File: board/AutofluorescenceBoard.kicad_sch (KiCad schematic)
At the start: 38 parts, among them U1 PAM2863ECR, U2 PAM2863ECR, U3 PAM2863ECR

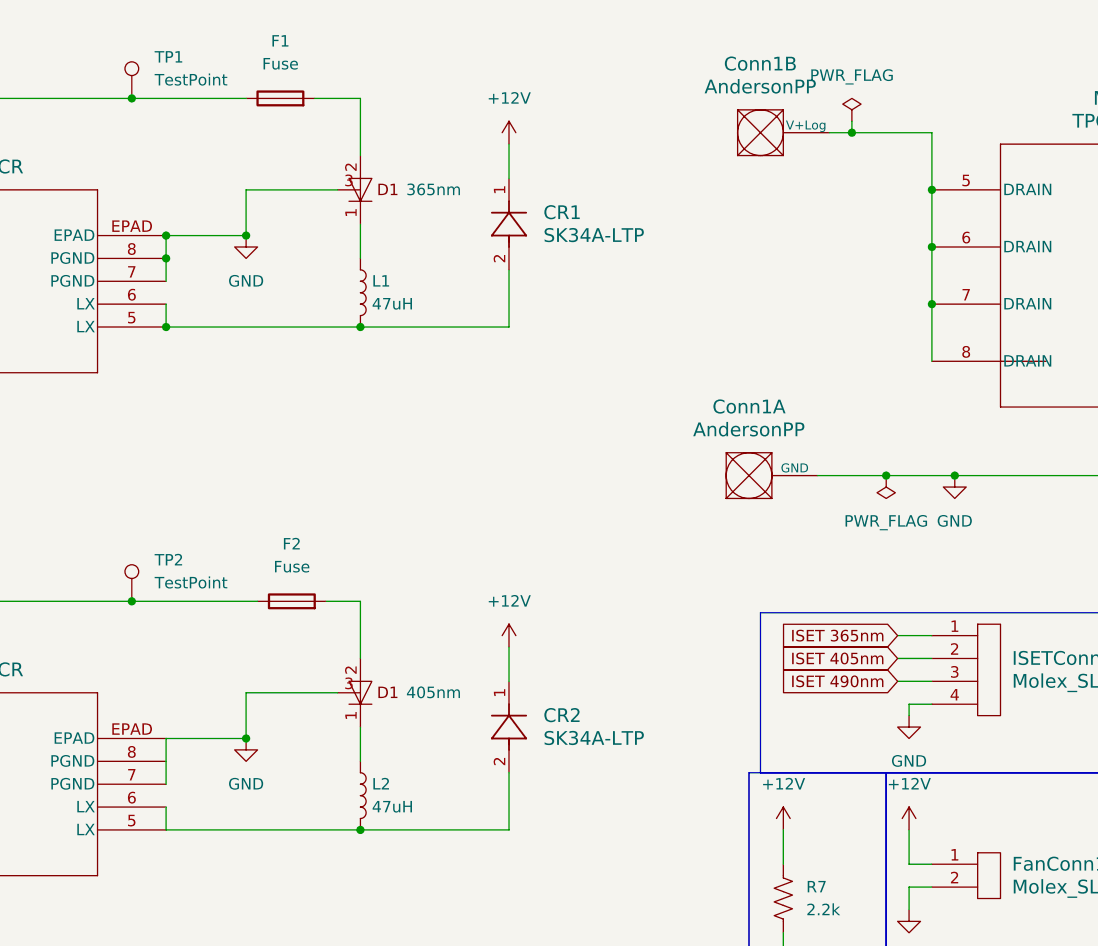
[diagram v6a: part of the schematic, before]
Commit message: Layout Ground Fixes
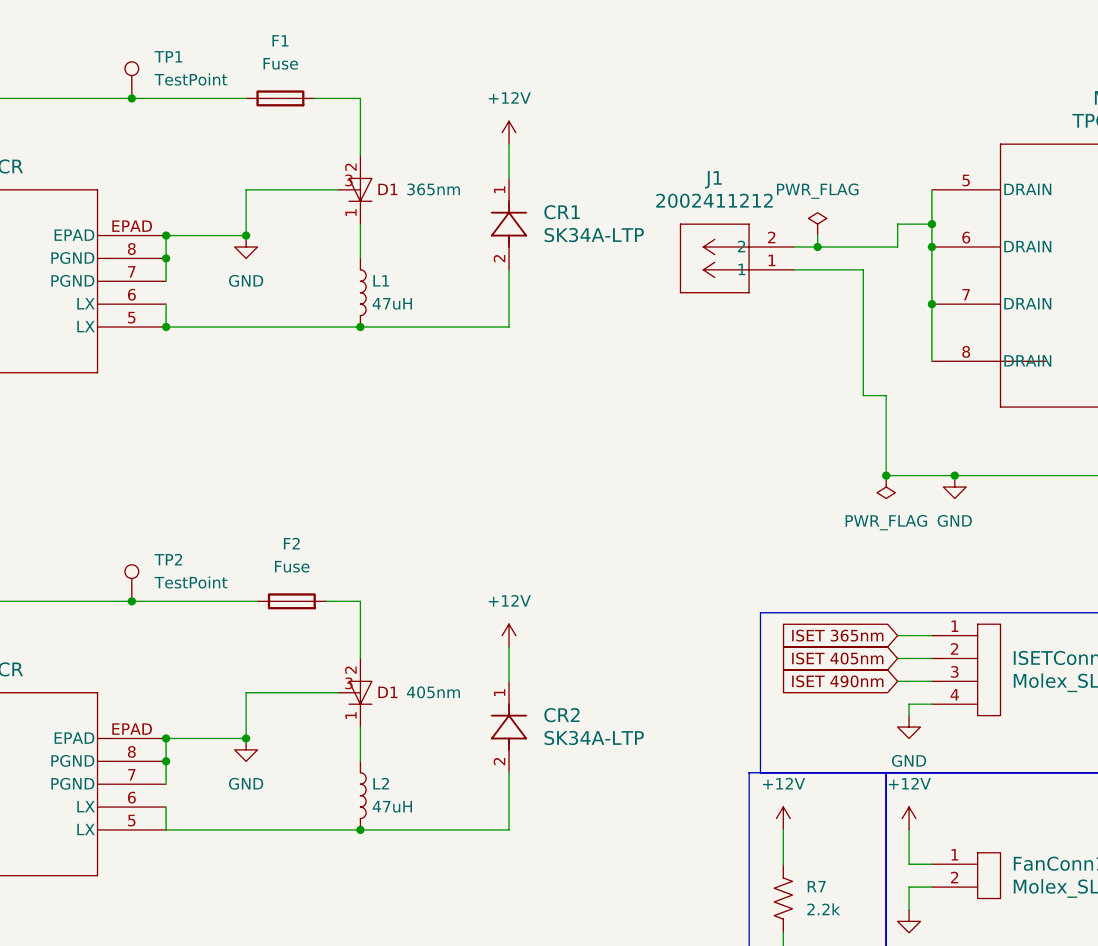
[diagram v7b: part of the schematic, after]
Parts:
- removed Conn1: AndersonPP, MRDT_Connectors:Square_Anderson_2_H_Side_By_Side, symbol MRDT_Connectors:AndersonPP
- added J1: 2002411212, CONN_2002412000_02_MOL, symbol AutofluorescenceBoard:2002411212
- FanConn1: footprint MRDT_Connectors:MOLEX_SL_02_Horizontal -> MRDT_Connectors:MOLEX_SL_02_Vertical
- ISETConn1: footprint MRDT_Connectors:MOLEX_SL_04_Horizontal -> MRDT_Connectors:MOLEX_SL_04_Vertical
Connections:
- net GND: now also U2.8 (PGND), J1.1
- net at MOSFET1.5 (DRAIN), MOSFET1.6 (DRAIN), MOSFET1.7 (DRAIN)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: now also J1.2

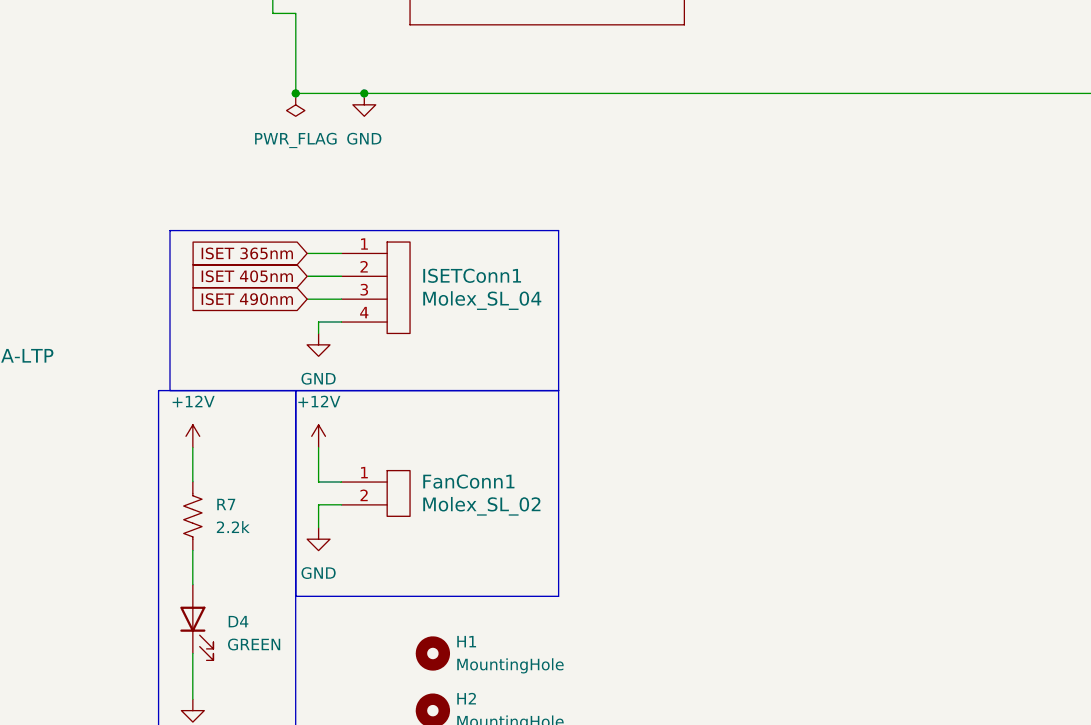
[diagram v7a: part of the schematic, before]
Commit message: Added White LED
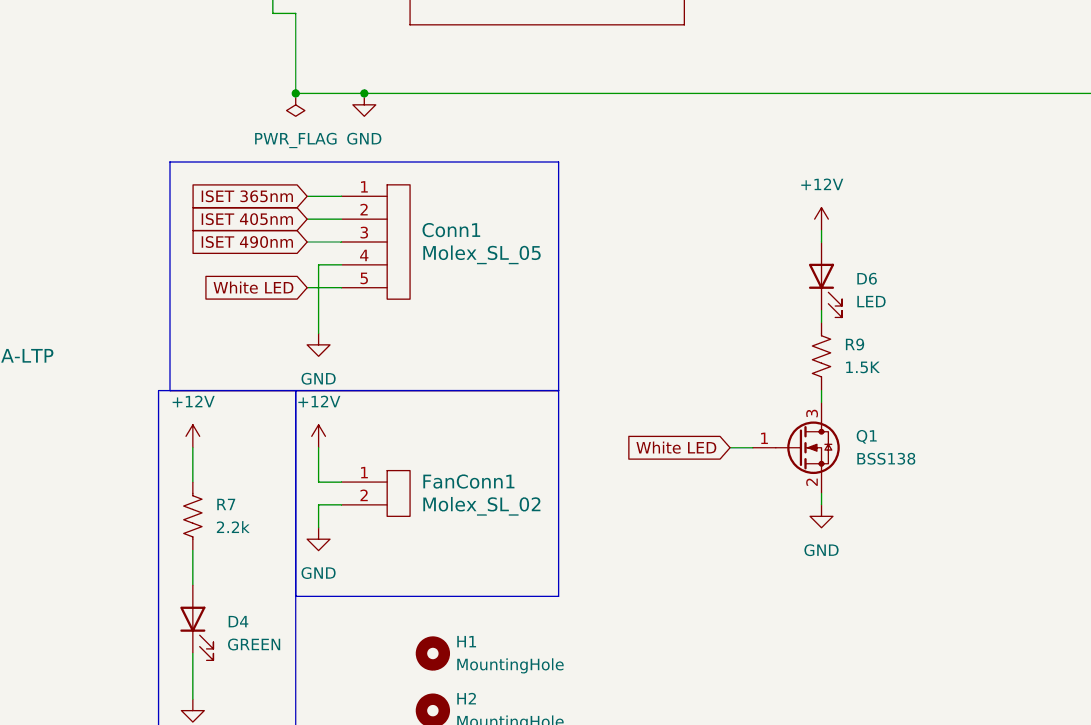
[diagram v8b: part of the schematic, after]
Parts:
- removed ISETConn1: Molex_SL_04, MRDT_Connectors:MOLEX_SL_04_Vertical, symbol MRDT_Connectors:Molex_SL_04
- added Conn1: Molex_SL_05, AutofluorescenceBoard:MOLEX_SL_05_Vertical_AF, symbol MRDT_Connectors:Molex_SL_05
- added D6: LED, AutofluorescenceBoard:INS63AT5UW, symbol Device:LED
- added Q1: BSS138, Package_TO_SOT_SMD:SOT-23, symbol Transistor_FET:BSS138
- added R9: 1.5K, AutofluorescenceBoard:RES_R0603_ROM-M, symbol Device:R_US
- FanConn1: footprint MRDT_Connectors:MOLEX_SL_02_Vertical -> AutofluorescenceBoard:MOLEX_SL_02_Horizontal
- J1: footprint CONN_2002412000_02_MOL -> AutofluorescenceBoard:CONN_SD-172286-1000_02_MOL
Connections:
- net +12V: now also D6.2 (A)
- net GND: now also Conn1.4, Q1.2 (S)
- net ISET 365nm: now also Conn1.1
- net ISET 405nm: now also Conn1.2
- net ISET 490nm: now also Conn1.3
- new net: D6.1 (K), R9.1
- new net: Q1.3 (D), R9.2
- new net White LED: Conn1.5, Q1.1 (G)
